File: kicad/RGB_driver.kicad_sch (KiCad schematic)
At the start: 17 parts, among them J1 USB_C_Receptacle_PowerOnly_6P, SW2 SW_Push_Open_Dual, SW3 SW_SPST, U3 ATtiny85-20P

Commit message: change: finished footprints layers, updated pcb with footprints - wip
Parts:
- removed J1: USB_C_Receptacle_PowerOnly_6P, symbol Connector:USB_C_Receptacle_PowerOnly_6P
- removed R1, R2: 5.1K, footprint_radiocontorler:resistor_footprint, symbol Device:R
- removed SW3: SW_SPST, symbol Switch:SW_SPST
- added J2: USB_C_Receptacle_USB2.0_16P, Connector_USB:USB_C_Receptacle_GCT_USB4105-xx-A_16P_TopMnt_Horizontal, symbol Connector:USB_C_Receptacle_USB2.0_16P
- added R3, R4: 5.1K, footprint_radiocontorler:resistor_footprint, symbol Device:R
- added SW4: SW_Push_Open_Dual, Button_Switch_THT:SW_PUSH_6mm, symbol Switch:SW_Push_Open_Dual
- C1, C2: footprint (none) -> Capacitor_THT:CP_Radial_D4.0mm_P1.50mm
- RV1: footprint (none) -> Potentiometer_THT:Potentiometer_ACP_CA6-H2,5_Horizontal
- SW2: footprint (none) -> Button_Switch_THT:SW_PUSH_6mm
- U2, U4, U5: footprint (none) -> footprint_radiocontorler:simple_generic_pad
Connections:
- net +5V: now also J2.A4 (VBUS), J2.A9 (VBUS), J2.B4 (VBUS), J2.B9 (VBUS)
- net GND: now also J2.A1 (GND), J2.A12 (GND), J2.B1 (GND), J2.B12 (GND), R3.2, R4.2, SW4.1
- net RST: now also SW4.2
- new net: J2.B5 (CC2), R4.1
- new net: J2.A5 (CC1), R3.1
- new net: J2.A6 (D+), J2.B6 (D+)
- new net: J2.A7 (D-), J2.B7 (D-)
- no-connect marks 2 -> 7

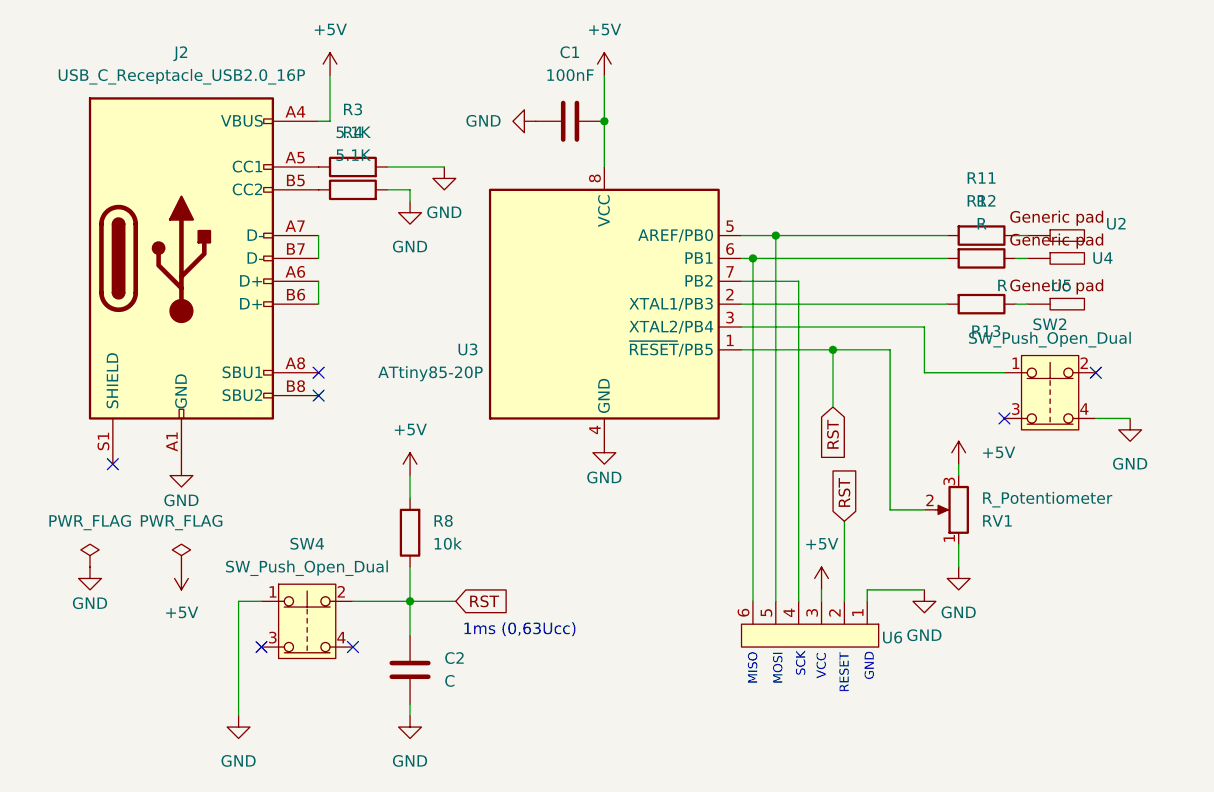
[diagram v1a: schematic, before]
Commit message: change: added footprints - button, potentiometer, fixed and connected pcb
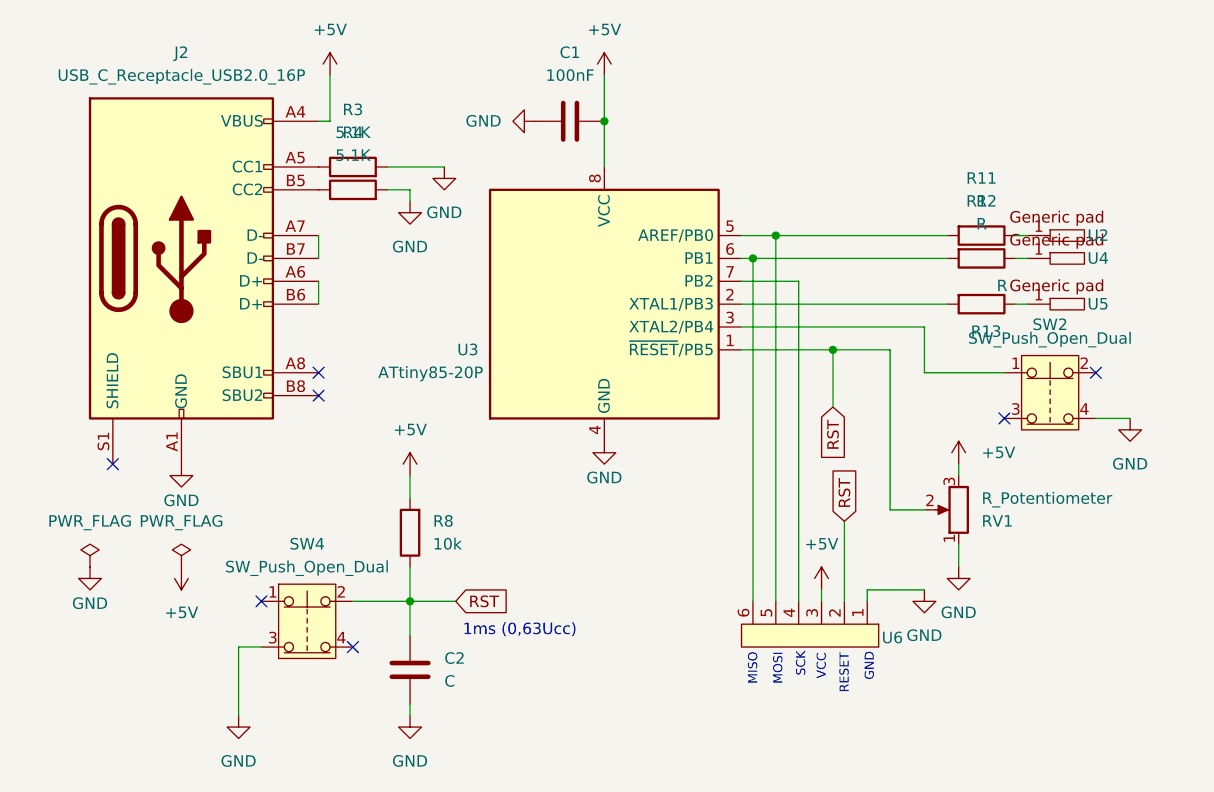
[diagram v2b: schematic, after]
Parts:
- RV1: footprint Potentiometer_THT:Potentiometer_ACP_CA6-H2,5_Horizontal -> footprint_radiocontorler:potentiometer_custom
- SW2, SW4: footprint Button_Switch_THT:SW_PUSH_6mm -> footprint_radiocontorler:a_long_button
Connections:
- net GND: now also SW4.3; no longer SW4.1
- net at R12.1: now also U4.1; no longer U4.
- net at R13.1: now also U5.1; no longer U5.
- net at R11.1: now also U2.1; no longer U2.
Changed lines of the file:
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@@
+	)
+	(no_connect
+		(at 69.85 106.68)
 	)
 	(no_connect
@@
 		(at 76.2 83.82)
 	)
-	(no_connect
-		(at 69.85 111.76)
-	)
 	(wire
 		(pts
@@
 	(wire
 		(pts
-			(xy 69.85 106.68) (xy 67.31 106.68)
+			(xy 67.31 111.76) (xy 69.85 111.76)
 		)
 		(stroke
@@
 	(wire
 		(pts
-			(xy 67.31 106.68) (xy 67.31 119.38)
+			(xy 67.31 111.76) (xy 67.31 119.38)
 		)
 		(stroke
@@
 		(dnp no)
 		(property "Reference" "U4"
-			(at 163.322 68.58 0)
+			(at 162.814 68.58 0)
 			(effects
 				(font
@@
 			)
 		)
-		(pin ""
+		(pin "1"
 		)
 		(instances
@@
 			)
 		)
-		(property "Footprint" "Button_Switch_THT:SW_PUSH_6mm"
+		(property "Footprint" "footprint_radiocontorler:a_long_button"
 			(at 157.48 76.2 0)
 			(effects
@@
 		(dnp no)
 		(property "Reference" "U2"
-			(at 164.846 64.77 0)
+			(at 162.814 66.04 0)
 			(effects
 				(font
@@
 		)
 		(property "Value" "~"
-			(at 158.242 60.96 0)
-			(effects
-				(font
-					(size 1.27 1.27)
-				)
+			(at 159.004 65.786 0)
+			(effects
+				(font
+					(size 1.27 1.27)
+				)
+				(hide yes)
 			)
 		)
@@
 			)
 		)
-		(pin ""
+		(pin "1"
 		)
 		(instances
@@
 			)
 		)
-		(property "Footprint" "Button_Switch_THT:SW_PUSH_6mm"
+		(property "Footprint" "footprint_radiocontorler:a_long_button"
 			(at 74.93 101.6 0)
 			(effects
@@
 			)
 		)
-		(property "Footprint" "Potentiometer_THT:Potentiometer_ACP_CA6-H2,5_Horizontal"
+		(property "Footprint" "footprint_radiocontorler:potentiometer_custom"
 			(at 147.32 96.52 0)
 			(effects
@@
 	)
 	(symbol
-		(lib_name "SPI_1")
 		(lib_id "Amplifier_Operational:SPI")
 		(at 139.7 110.49 270)
@@
 		(dnp no)
 		(property "Reference" "U5"
-			(at 158.75 71.628 0)
+			(at 162.814 73.66 0)
 			(effects
 				(font
@@
 			)
 		)
-		(pin ""
-		)
-		(instances
+		(pin "1"
+		)
+		(instances

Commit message: change: corrected button size, reorganized pcb
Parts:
- SW2, SW4: footprint footprint_radiocontorler:a_long_button -> footprint_radiocontorler:a_huge_button
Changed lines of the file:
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@@
 			)
 		)
-		(property "Footprint" "footprint_radiocontorler:a_long_button"
+		(property "Footprint" "footprint_radiocontorler:a_huge_button"
 			(at 157.48 76.2 0)
 			(effects
@@
 			)
 		)
-		(property "Footprint" "footprint_radiocontorler:a_long_button"
+		(property "Footprint" "footprint_radiocontorler:a_huge_button"
 			(at 74.93 101.6 0)
 			(effects

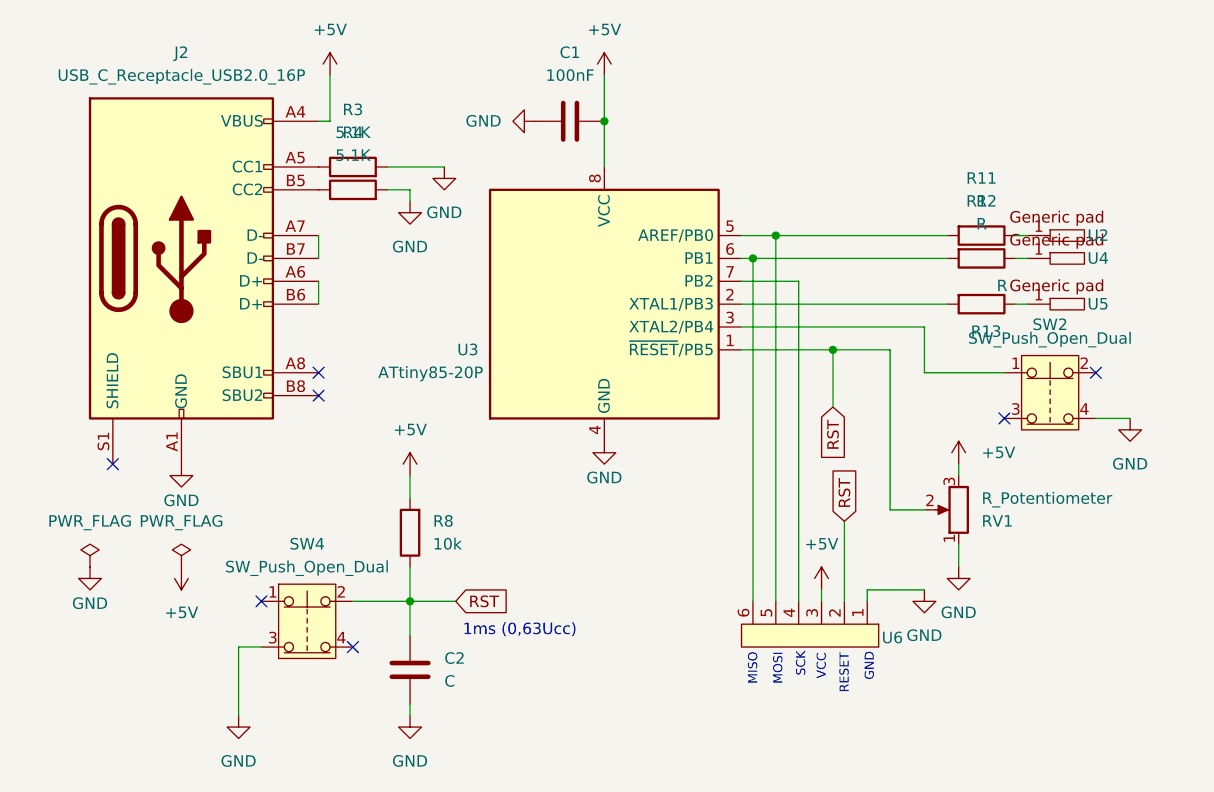
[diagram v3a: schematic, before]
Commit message: fix: reset, spi, main button and potentiometer changed pins and connections, no capacitor on reset, ceramic capacitor at vcc
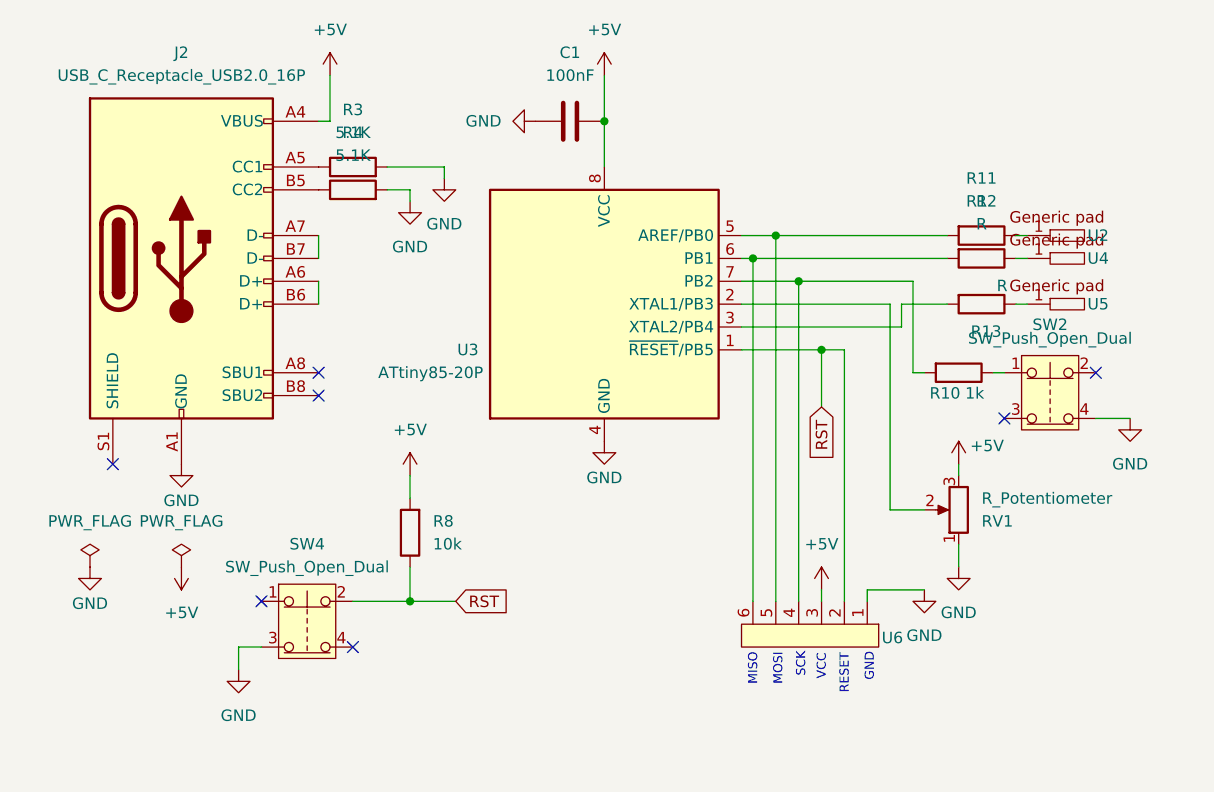
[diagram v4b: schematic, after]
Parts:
- removed C2: C, Capacitor_THT:CP_Radial_D4.0mm_P1.50mm, symbol Device:C
- added R10: 1k, footprint_radiocontorler:resistor_footprint, symbol Device:R
- C1: footprint Capacitor_THT:CP_Radial_D4.0mm_P1.50mm -> Capacitor_THT:C_Disc_D7.0mm_W2.5mm_P5.00mm
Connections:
- net RST: no longer RV1.2
- net at R13.2: now also U3.3 (XTAL2/PB4); no longer U3.2 (XTAL1/PB3)
- net at SW2.1: now also R10.1; no longer U3.3 (XTAL2/PB4)
- net at U3.7 (PB2), U6.4: now also R10.2
- new net: RV1.2, U3.2 (XTAL1/PB3)
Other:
- note removed: "1ms (0,63Ucc)"

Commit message: fix: power supply for reset removed, new gerber files
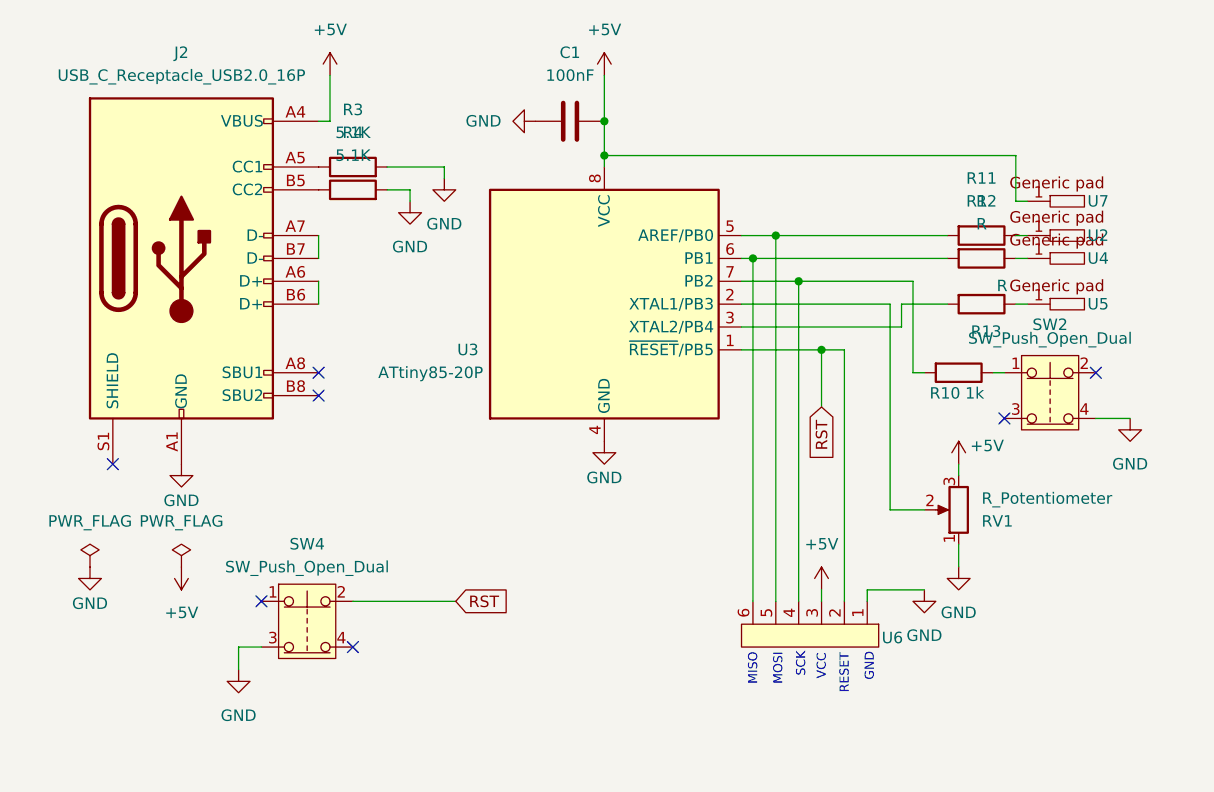
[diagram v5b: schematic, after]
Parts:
- removed R8: 10k, footprint_radiocontorler:resistor_footprint, symbol Device:R
- added U7: ~, footprint_radiocontorler:simple_generic_pad, symbol Amplifier_Operational:generic_pad
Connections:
- net +5V: now also U7.1
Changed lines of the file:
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@@
+	)
+	(junction
+		(at 107.95 57.15)
+		(diameter 0)
+		(color 0 0 0 0)
 	)
 	(junction
@@
 	)
 	(junction
-		(at 86.36 106.68)
-		(diameter 0)
-		(color 0 0 0 0)
-	)
-	(junction
 		(at 127 66.04)
 		(diameter 0)
@@
 	(wire
 		(pts
+			(xy 107.95 57.15) (xy 107.95 58.42)
+		)
+		(stroke
+			(width 0)
+			(type default)
+		)
+	)
+	(wire
+		(pts
 			(xy 124.46 68.58) (xy 124.46 106.68)
 		)
@@
 	(wire
 		(pts
-			(xy 80.01 106.68) (xy 86.36 106.68)
+			(xy 80.01 106.68) (xy 91.44 106.68)
 		)
 		(stroke
@@
 	(wire
 		(pts
-			(xy 86.36 92.71) (xy 86.36 95.25)
-		)
-		(stroke
-			(width 0)
-			(type default)
-		)
-	)
-	(wire
-		(pts
 			(xy 67.31 111.76) (xy 67.31 114.3)
 		)
@@
 	(wire
 		(pts
-			(xy 86.36 102.87) (xy 86.36 106.68)
+			(xy 153.67 62.23) (xy 154.94 62.23)
 		)
 		(stroke
@@
 	(wire
 		(pts
+			(xy 107.95 57.15) (xy 153.67 57.15)
+		)
+		(stroke
+			(width 0)
+			(type default)
+		)
+	)
+	(wire
+		(pts
 			(xy 77.47 53.34) (xy 77.47 48.26)
 		)
@@
 	(wire
 		(pts
+			(xy 153.67 57.15) (xy 153.67 62.23)
+		)
+		(stroke
+			(width 0)
+			(type default)
+		)
+	)
+	(wire
+		(pts
 			(xy 153.67 73.66) (xy 154.94 73.66)
 		)
@@
 	(wire
 		(pts
-			(xy 86.36 106.68) (xy 91.44 106.68)
-		)
-		(stroke
-			(width 0)
-			(type default)
-		)
-	)
-	(wire
-		(pts
-			(xy 107.95 53.34) (xy 107.95 58.42)
+			(xy 107.95 53.34) (xy 107.95 57.15)
 		)
 		(stroke
@@
 	(symbol
 		(lib_id "Device:R")
-		(at 86.36 99.06 180)
-		(unit 1)
-		(exclude_from_sim no)
-		(in_bom yes)
-		(on_board yes)
-		(dnp no)
-		(fields_autoplaced yes)
-		(property "Reference" "R8"
-			(at 88.9 97.7899 0)
-			(effects
-				(font
-					(size 1.27 1.27)
-				)
-				(justify right)
-			)
-		)
-		(property "Value" "10k"
-			(at 88.9 100.3299 0)
-			(effects
-				(font
-					(size 1.27 1.27)
-				)
-				(justify right)
-			)
-		)
-		(property "Footprint" "footprint_radiocontorler:resistor_footprint"
-			(at 88.138 99.06 90)
-			(effects
-				(font
-					(size 1.27 1.27)
-				)
-				(hide yes)
-			)
-		)
-		(property "Datasheet" "~"
-			(at 86.36 99.06 0)
-			(effects
-				(font
-					(size 1.27 1.27)
-				)
-				(hide yes)
-			)
-		)
-		(property "Description" "Resistor"
-			(at 86.36 99.06 0)
-			(effects
-				(font
-					(size 1.27 1.27)
-				)
-				(hide yes)
-			)
-		)
-		(pin "2"
-		)
-		(pin "1"
-		)
-		(instances
-			(project "RGB_driver"
-				(path "/1ccb5a9c-254c-4919-974f-8891fcdc32e1"
-					(reference "R8")
-					(unit 1)
-				)
-			)
-		)
-	)
-	(symbol
-		(lib_id "Device:R")
 		(at 149.86 73.66 270)
 		(unit 1)
@@
 	)
 	(symbol
-		(lib_id "power:+5V")
-		(at 86.36 92.71 0)
-		(unit 1)
-		(exclude_from_sim no)
-		(in_bom yes)
-		(on_board yes)
-		(dnp no)
-		(fields_autoplaced yes)
-		(property "Reference" "#PWR09"
-			(at 86.36 96.52 0)
-			(effects
-				(font
-					(size 1.27 1.27)
-				)
-				(hide yes)
-			)
-		)
-		(property "Value" "+5V"
-			(at 86.36 87.63 0)
-			(effects
-				(font
-					(size 1.27 1.27)
-				)
-			)
-		)
-		(property "Footprint" ""
-			(at 86.36 92.71 0)
-			(effects
-				(font
-					(size 1.27 1.27)
-				)
-				(hide yes)
-			)
-		)
-		(property "Datasheet" ""
-			(at 86.36 92.71 0)
-			(effects
-				(font
-					(size 1.27 1.27)
-				)
-				(hide yes)
-			)
-		)
-		(property "Description" "Power symbol creates a global label with name \"+5V\""
-			(at 86.36 92.71 0)
-			(effects
-				(font
-					(size 1.27 1.27)
-				)
-				(hide yes)
-			)
-		)
-		(pin "1"
-		)
-		(instances
-			(project "RGB_driver"
-				(path "/1ccb5a9c-254c-4919-974f-8891fcdc32e1"
-					(reference "#PWR09")
-					(unit 1)
-				)
-			)
-		)
-	)
-	(symbol
 		(lib_id "Connector:USB_C_Receptacle_USB2.0_16P")
 		(at 60.96 68.58 0)
@@
 					(unit 1)
 				)
+			)
+		)
+	)
+	(symbol
+		(lib_id "Amplifier_Operational:generic_pad")
+		(at 158.75 62.23 0)
+		(unit 1)
+		(exclude_from_sim no)
+		(in_bom yes)
+		(on_board yes)
+		(dnp no)
+		(property "Reference" "U7"
+			(at 162.814 62.23 0)
+			(effects
+				(font
+					(size 1.27 1.27)
+				)
+			)
+		)
+		(property "Value" "~"
+			(at 158.242 57.15 0)
+			(effects
+				(font
+					(size 1.27 1.27)
+				)
+			)
+		)
+		(property "Footprint" "footprint_radiocontorler:simple_generic_pad"
+			(at 158.75 62.23 0)
+			(effects
+				(font
+					(size 1.27 1.27)
+				)
+				(hide yes)
+			)
+		)
+		(property "Datasheet" ""
+			(at 158.75 62.23 0)
+			(effects
+				(font
+					(size 1.27 1.27)
+				)
+				(hide yes)
+			)
+		)
+		(property "Description" ""
+			(at 158.75 62.23 0)
+			(effects
+				(font
+					(size 1.27 1.27)
+				)
+				(hide yes)
+			)
+		)
+		(pin "1"
+		)
+		(instances
+			(project "RGB_driver"
+				(path "/1ccb5a9c-254c-4919-974f-8891fcdc32e1"
+					(reference "U7")
+					(unit 1)
+				)
